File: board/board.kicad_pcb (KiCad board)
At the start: 4 copper layers, 45 x 29 mm, 46 parts, among them J1 015_RGMII, J2 020_1000BASE-T_with_CT, J3 Conn_01x03_Male, U2 TLV71209_SOT23-5, Y1 Crystal_GND24_Small

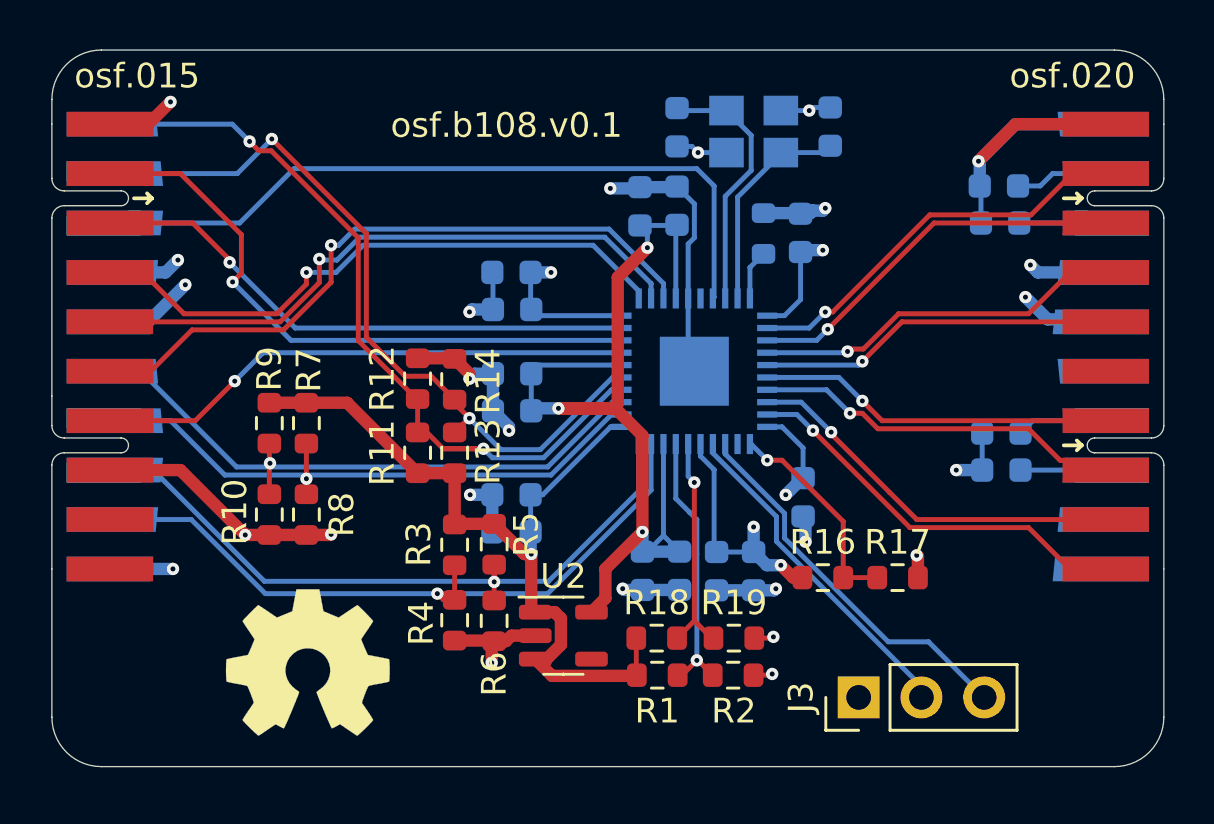
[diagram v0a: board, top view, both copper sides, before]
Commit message: optimized EMI
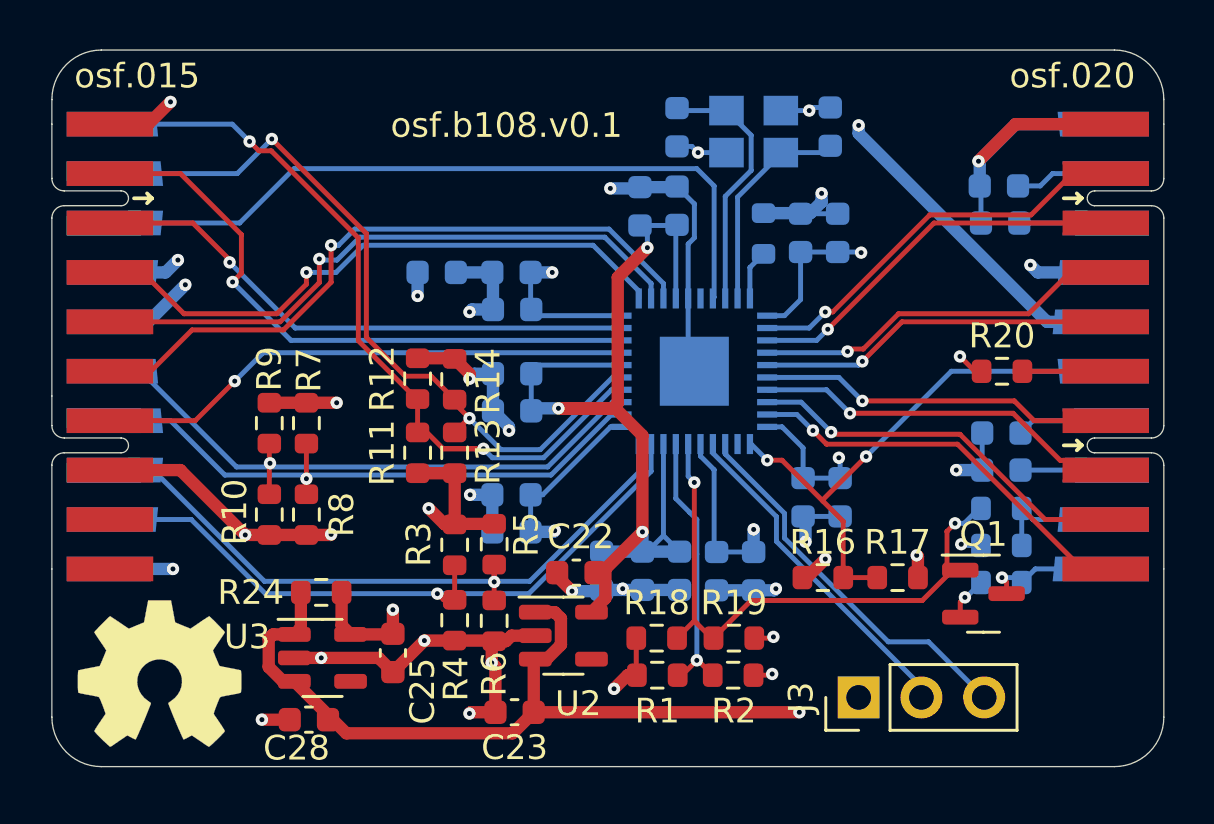
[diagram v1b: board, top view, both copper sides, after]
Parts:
- added C21: 4.7uF, Capacitor_SMD:C_0603_1608Metric, B.Cu at (162.2, 111.1)
- added C22: 4.7uF, Capacitor_SMD:C_0603_1608Metric, F.Cu at (161.2, 111.2)
- added C23: 4.7uF, Capacitor_SMD:C_0603_1608Metric, F.Cu at (158.7, 116.8)
- added C24: 4.7uF, Capacitor_SMD:C_0603_1608Metric, B.Cu at (155.6, 99.0)
- added C25: 4.7uF, Capacitor_SMD:C_0603_1608Metric, F.Cu at (153.8, 114.4)
- added C26: 10nF, Capacitor_SMD:C_0603_1608Metric, B.Cu at (171.9, 108.1)
- added C27: 10nF, Capacitor_SMD:C_0603_1608Metric, B.Cu at (171.8, 97.4)
- added C28: 4.7uF, Capacitor_SMD:C_0603_1608Metric, F.Cu at (150.4, 117.1)
- added Q1: FDV301N, Package_TO_SOT_SMD:SOT-23, F.Cu at (177.7, 112.0)
- added R20: 49.9R, Resistor_SMD:R_0603_1608Metric, F.Cu at (178.4, 103.0)
- added R21: 49.9R, Resistor_SMD:R_0603_1608Metric, B.Cu at (178.4, 110.0)
- added R22: d.n.p, Resistor_SMD:R_0603_1608Metric, B.Cu at (178.4, 108.5)
- added R23: d.n.p, Resistor_SMD:R_0603_1608Metric, B.Cu at (178.4, 111.5)
- added R24: d.n.p, Resistor_SMD:R_0603_1608Metric, F.Cu at (150.9, 112.0)
- added U3: TLV71318PQDBVRQ1, Package_TO_SOT_SMD:SOT-23-5, F.Cu at (150.9, 114.6)
- R10, R11, R14, R17, R18, R2, R4, R6, R8: value 10k -> d.n.p
- U1: value (none) -> ADIN1300BCPZ
- moved LOGO1 6.02 mm to (144.3, 115.2)
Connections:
- net Net-(R18-Pad2) renamed /ADIN1300/ETH1_LED_LINK
- C10 pad 1: /ADIN1300/VDD -> /ADIN1300/VDDIO
- C11 pad 1: /ADIN1300/VDD -> /ADIN1300/VDDIO
- C12 pad 1: /ADIN1300/VDD -> /ADIN1300/VDDIO
- C13 pad 1: /ADIN1300/VDD -> +3.3V
- C15 pad 1: /ADIN1300/VDD -> +3.3V
- C7 pad 1: /ADIN1300/VDD -> /ADIN1300/VDDIO
- C8 pad 1: /ADIN1300/VDD -> /ADIN1300/VDDIO
- C9 pad 1: /ADIN1300/VDD -> /ADIN1300/VDDIO
- J2 pad 16: unconnected-(J2-Pad16) -> /LED1_C
- J2 pad 19: unconnected-(J2-Pad19) -> /LED2_A
- J2 pad 20: unconnected-(J2-Pad20) -> /LED2_C
- J2 pad 6: unconnected-(J2-Pad6) -> /LED1_A
- R1 pad 1: /ADIN1300/VDD -> /ADIN1300/VDDIO
- R11 pad 1: /ADIN1300/VDD -> /ADIN1300/VDDIO
- R13 pad 1: /ADIN1300/VDD -> /ADIN1300/VDDIO
- R16 pad 1: /ADIN1300/VDD -> +3.3V
- R16 pad 2: Net-(R16-Pad2) -> /LED1_C
- R17 pad 1: Net-(R16-Pad2) -> /LED1_C
- R18 pad 1: /ADIN1300/VDD -> /ADIN1300/VDDIO
- R3 pad 1: /ADIN1300/VDD -> /ADIN1300/VDDIO
- R5 pad 1: /ADIN1300/VDD -> /ADIN1300/VDDIO
- R7 pad 1: /ADIN1300/VDD -> /ADIN1300/VDDIO
- R9 pad 1: /ADIN1300/VDD -> /ADIN1300/VDDIO
- U1 pad 11: /ADIN1300/VDD -> +3.3V
- U1 pad 20: /ADIN1300/VDD -> +3.3V
- U1 pad 21: Net-(R16-Pad2) -> /LED1_C
- U1 pad 25: /ADIN1300/VDD -> /ADIN1300/VDDIO
- U1 pad 31: /ADIN1300/VDD -> /ADIN1300/VDDIO
- U1 pad 40: /ADIN1300/VDD -> /ADIN1300/VDDIO
- U2 pad 1: /ADIN1300/VDD -> +3.3V
- U2 pad 3: /ADIN1300/VDD -> +3.3V
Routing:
- net /ADIN1300/VDD: track 91.1 -> 0.00 mm, vias 6 -> 0
- net +3.3V: track 46.7 -> 93.9 mm, vias 2 -> 8
- net /ADIN1300/VDDIO: track 0.00 -> 37.9 mm, vias 0 -> 8
- net GND: track 149.6 -> 172.9 mm, vias 21 -> 27
- net /LED1_C: track 0.00 -> 22.3 mm, vias 0 -> 2
- net /ADIN1300/ETH1_LED_LINK: track 9.31 -> 23.9 mm, vias 1 -> 2
- net Net-(R16-Pad2): track 8.72 -> 0.00 mm, vias 1 -> 0
- net /LED2_C: track 0.00 -> 5.09 mm, vias 0 -> 1
- net /LED2_A: track 0.00 -> 5.04 mm
- net /LED1_A: track 0.00 -> 3.38 mm
- net /ADIN1300/DVDD: track 41.2 -> 42.8 mm
- added copper zone on In1.Cu, net +3.3V
- added copper zone on In1.Cu, net /ADIN1300/VDDIO

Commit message: specified crystal frequentcy
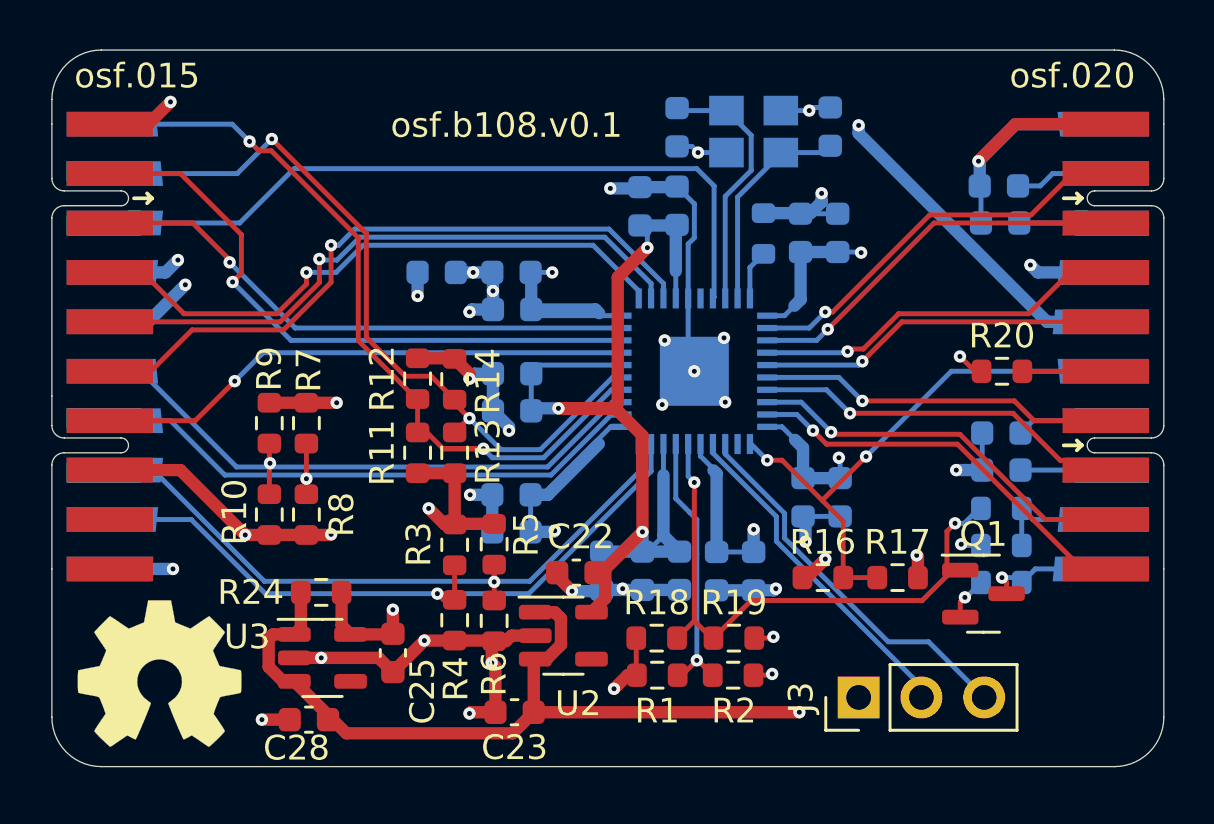
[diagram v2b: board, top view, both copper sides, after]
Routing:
- net /ADIN1300/VDDIO: track 37.9 -> 47.7 mm
- net GND: vias 27 -> 34
